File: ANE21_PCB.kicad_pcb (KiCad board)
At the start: 2 copper layers, 128 parts, among them J1 Conn_02x07_Odd_Even, J11 Conn_02x05_Odd_Even, J12 THD-02-R, J13 1-2199119-5, J14 USB_A, J15 USB_OTG, J2 Conn_01x03, J3 Conn_01x03, J4 THD-20-R, J5 690-019-298-412, J8 Molex 470531000, Q1 DMP3013SFV-7, U1 74LVC1G07SE-7, U10 TPD4EUSB30, U11 AP22653W6, U12 SI-51005-F, U13 RT9742SNGV, U2 74LVC1G07SE-7, U4 AP64501SP-13, U5 PCF85063AT/AAZ, U6 EMC2301-1-ACZL-TR, U7 74LVC1G07SE-7, U8 FSUSB42MUX, U9 USB2514B-I/M2, Y1 24MHz, Y2 X32K768S301

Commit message: Added 3d-models, esd protection, cleaned up and made small start with pcb
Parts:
- removed BT1: Battery_Cell, Battery:BatteryHolder_Keystone_3034_1x20mm
- removed C15, C31, C32, C33, C34, C42, C43, C50, C52, C53, C54, C55: 10u, Capacitor_SMD:C_0805_2012Metric
- removed C16, C35, C51: 100uF, Capacitor_Tantalum_SMD:CP_EIA-7343-31_Kemet-D
- removed C17, C18, C19, C20, C22, C23, C27: 10u 35v, Capacitor_SMD:C_0805_2012Metric
- removed C21: 100n 100v, Capacitor_SMD:C_0402_1005Metric
- removed C24, C25, C26, C36, C37, C38, C39, C44, C45, C46, C47, C48, C49: 100n, Capacitor_SMD:C_0402_1005Metric
- removed C28, C30: nf, Capacitor_SMD:C_0402_1005Metric
- removed C29: 1.2nF, Capacitor_SMD:C_0402_1005Metric
- removed C40, C41: 27pF, Capacitor_SMD:C_0402_1005Metric
- removed D2: BAT54C-7-F, Package_TO_SOT_SMD:SOT-23
- removed J11: Conn_02x05_Odd_Even, Connector_PinHeader_2.54mm:PinHeader_2x05_P2.54mm_Vertical
- removed J12: THD-02-R, Connector_PinHeader_2.54mm:PinHeader_2x02_P2.54mm_Vertical
- removed J14: USB_A, Connector_USB:USB_A_Receptacle_XKB_U231-091N-4BLRA00-S
- removed J2: Conn_01x03, Connector_PinHeader_2.54mm:PinHeader_1x03_P2.54mm_Vertical
- removed J8: Molex 470531000, Connector:FanPinHeader_1x04_P2.54mm_Vertical
- removed Module2: ComputeModule4-CM4, ComputeModule4:Raspberry-Pi-4-Compute-Module
- removed Q1: DMP3013SFV-7, Package_SON:Diodes_PowerDI3333-8
- removed R10, R17, R19: 36K 1%, Resistor_SMD:R_0402_1005Metric
- removed R11, R12: 510K 1%, Resistor_SMD:R_0402_1005Metric
- removed R13, R14, R21, R22, R9: 2.2K 1%, Resistor_SMD:R_0402_1005Metric
- removed R18, R8: 12K 1%, Resistor_SMD:R_0402_1005Metric
- removed R20: 15K 1%, Resistor_SMD:R_0402_1005Metric
- removed R7: 20K 1%, Resistor_SMD:R_0402_1005Metric
- removed TP1, TP2, TP3, TP4: TestPoint, TestPoint:TestPoint_Pad_2.0x2.0mm
- removed U5: PCF85063AT/AAZ, Package_SO:SOIC-8_3.9x4.9mm_P1.27mm
- removed U6: EMC2301-1-ACZL-TR, Package_SO:MSOP-8_3x3mm_P0.65mm
- removed U7: 74LVC1G07SE-7, Package_TO_SOT_SMD:SOT-353_SC-70-5
- removed Y1: 24MHz, Crystal:Crystal_SMD_HC49-SD
- removed Y2: X32K768S301, Crystal:Crystal_SMD_3215-2Pin_3.2x1.5mm
- added C59: 100n, Capacitor_SMD:C_0603_1608Metric, F.Cu at (129.6, 72.4)
- added J16: Conn_01x02, Connector_PinHeader_2.54mm:PinHeader_1x02_P2.54mm_Vertical, F.Cu at (150.8, 65.9)
- added J6: SS-52400-004, SS-52400-004 (USB-c connector):STEWART_SS-52400-004 (USB-C), F.Cu at (112.0, 50.3)
- added Module1: ComputeModule4-CM4, ComputeModule4:Raspberry-Pi-4-Compute-Module, F.Cu at (114.4, 126.4)
- added U3: HUSB238_xxxDD, Package_DFN_QFN:WDFN-10-1EP_3x3mm_P0.5mm_EP1.8x2.5mm, F.Cu at (112.5, 59.3)
- C1, C6: value 10u 35v -> 100nF; footprint Capacitor_SMD:C_0805_2012Metric -> Capacitor_SMD:C_0603_1608Metric
- C10: value 1.2nF -> 22uF; footprint Capacitor_SMD:C_0402_1005Metric -> Capacitor_SMD:C_0603_1608Metric
- C11: value nf -> 22uF; footprint Capacitor_SMD:C_0402_1005Metric -> Capacitor_SMD:C_0603_1608Metric
- C12, C13: value 10u -> 22uF; footprint Capacitor_SMD:C_0805_2012Metric -> Capacitor_SMD:C_0603_1608Metric
- C14: value 10u -> 100nF; footprint Capacitor_SMD:C_0805_2012Metric -> Capacitor_SMD:C_0603_1608Metric
- C2: value 10u 35v -> 22µF; footprint Capacitor_SMD:C_0805_2012Metric -> Capacitor_SMD:C_0603_1608Metric
- C3: value 10u 35v -> 1µF; footprint Capacitor_SMD:C_0805_2012Metric -> Capacitor_SMD:C_0603_1608Metric
- C4, C5: value 10u 35v -> 10µF; footprint Capacitor_SMD:C_0805_2012Metric -> Capacitor_SMD:C_0603_1608Metric
- C56, C57: footprint Capacitor_SMD:C_0402_1005Metric -> Capacitor_SMD:C_0603_1608Metric
- C7: value 100n -> 100nF; footprint Capacitor_SMD:C_0402_1005Metric -> Capacitor_SMD:C_0603_1608Metric
- C8: value 100n -> 10pF; footprint Capacitor_SMD:C_0402_1005Metric -> Capacitor_SMD:C_0603_1608Metric
- C9: value nf -> 10pF; footprint Capacitor_SMD:C_0402_1005Metric -> Capacitor_SMD:C_0603_1608Metric
- J1: value Conn_02x07_Odd_Even -> Conn_02x05_Odd_Even
- J3: value Conn_01x03 -> USB-A-S-VT; footprint Connector_PinHeader_2.54mm:PinHeader_1x03_P2.54mm_Vertical -> USB-A-S-VT:CONN_USB-A-S-VT_ADM
- L1, L2: value SRN6045TA-3R3Y -> 3,3uH; footprint Inductor_SMD:L_Bourns_SRN6045TA -> Inductor_SMD:L_0603_1608Metric
- R1, R6: value 10R -> 10K; footprint Resistor_SMD:R_0402_1005Metric -> Resistor_SMD:R_0603_1608Metric
- R15, R16: value 36K 1% -> 330; footprint Resistor_SMD:R_0402_1005Metric -> Resistor_SMD:R_0603_1608Metric
- R2: value 12K 1% -> 22.6K; footprint Resistor_SMD:R_0402_1005Metric -> Resistor_SMD:R_0603_1608Metric
- R23, R26: footprint Resistor_SMD:R_0402_1005Metric -> Resistor_SMD:R_0603_1608Metric
- R3: value 47K 1% -> 31,6K; footprint Resistor_SMD:R_0402_1005Metric -> Resistor_SMD:R_0603_1608Metric
- R4: value 15K 1% -> 10K; footprint Resistor_SMD:R_0402_1005Metric -> Resistor_SMD:R_0603_1608Metric
- R5: value 12K 1% -> 52,3K; footprint Resistor_SMD:R_0402_1005Metric -> Resistor_SMD:R_0603_1608Metric
- U10: value TPD4EUSB30 -> PUSB3FR4; footprint Package_SON:USON-10_2.5x1.0mm_P0.5mm -> lib:SOT1176-1
- U11: value AP22653W6 -> TPD4EUSB30; footprint Package_TO_SOT_SMD:SOT-23-6 -> Package_SON:USON-10_2.5x1.0mm_P0.5mm
- U12: footprint Ethernet_con:TE_RJ45-8L-B -> SI-51005-F:BEL_SI-51005-F
- U4: value AP64501SP-13 -> AP62300WU-7; footprint Package_SO:SOIC-8-1EP_3.9x4.9mm_P1.27mm_EP2.95x4.9mm_Mask2.71x3.4mm_ThermalVias -> AP62300WU-7:SOT95P280X100-6N
- U8: value FSUSB42MUX -> AP62300WU-7; footprint Package_SO:MSOP-10_3x3mm_P0.5mm -> AP62300WU-7:SOT95P280X100-6N
- U9: value USB2514B-I/M2 -> PUSB3FR4; footprint Package_DFN_QFN:QFN-36-1EP_6x6mm_P0.5mm_EP3.7x3.7mm -> lib:SOT1176-1
- moved J4 115.6 mm to (-89.9, 43.4)
- moved J15 111.1 mm to (153.0, 72.5), turned to 90 degrees
- moved J13 102.1 mm to (72.7, 54.3)
- moved U11 92.6 mm to (146.7, 67.8), turned to 180 degrees
- moved U1 85.2 mm to (22.2, 47.4)
- moved U12 84.2 mm to (129.3, 56.0)
- moved U10 79.9 mm to (138.1, 83.0)
- moved J1 79.4 mm to (15.2, 33.9)
- moved U13 74.5 mm to (101.5, 60.9), turned to -90 degrees
- moved R16 73.3 mm to (132.5, 72.0), turned to 90 degrees
- moved C57 70.0 mm to (99.2, 60.9), turned to -90 degrees
- moved U8 67.8 mm to (112.5, 72.9), turned to 180 degrees
- moved C56 67.0 mm to (103.8, 60.9), turned to -90 degrees
- moved H5 66.4 mm to (37.4, 35.0)
- moved H6 66.4 mm to (37.4, 42.0)
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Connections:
- net /GPIO10 renamed /CM4_LowSpeed/GPIO10
- net /GPIO11 renamed /CM4_LowSpeed/GPIO11
- net /GPIO12 renamed /CM4_LowSpeed/GPIO12
- net /GPIO13 renamed /CM4_LowSpeed/GPIO13
- net /GPIO14 renamed /CM4_LowSpeed/GPIO14
- net /GPIO15 renamed /CM4_LowSpeed/GPIO15
- net /GPIO16 renamed /CM4_LowSpeed/GPIO16
- net /GPIO17 renamed /CM4_LowSpeed/GPIO17
- net /GPIO18 renamed /CM4_LowSpeed/GPIO18
- net /GPIO19 renamed /CM4_LowSpeed/GPIO19
- net /GPIO2 renamed /CM4_LowSpeed/GPIO2
- net /GPIO20 renamed /CM4_LowSpeed/GPIO20
- net /GPIO21 renamed /CM4_LowSpeed/GPIO21
- net /GPIO22 renamed /CM4_LowSpeed/GPIO22
- net /GPIO23 renamed /CM4_LowSpeed/GPIO23
- net /GPIO24 renamed /CM4_LowSpeed/GPIO24
- net /GPIO25 renamed /CM4_LowSpeed/GPIO25
- net /GPIO26 renamed /CM4_LowSpeed/GPIO26
- net /GPIO27 renamed /CM4_LowSpeed/GPIO27
- net /GPIO3 renamed /CM4_LowSpeed/GPIO3
- net /GPIO4 renamed /CM4_LowSpeed/GPIO4
- net /GPIO5 renamed /CM4_LowSpeed/GPIO5
- net /GPIO6 renamed /CM4_LowSpeed/GPIO6
- net /GPIO7 renamed /CM4_LowSpeed/GPIO7
- net /GPIO8 renamed /CM4_LowSpeed/GPIO8
- net /GPIO9 renamed /CM4_LowSpeed/GPIO9
- net /ID_SC renamed /CM4_LowSpeed/ID_SC
- net /ID_SD renamed /CM4_LowSpeed/ID_SD
- C1 pad 1: /+12v -> GND
- C1 pad 2: GND -> VIN_U9
- C10 pad 1: Net-(C10-Pad1) -> GND
- C10 pad 2: GND -> +3,3V DC
- C11 pad 1: /PSUs/+3.3v -> GND
- C11 pad 2: Net-(U3-FB) -> +5V DC
- C12 pad 1: /PSUs/+3.3v -> GND
- C12 pad 2: GND -> +3,3V DC
- C13 pad 1: /PSUs/+3.3v -> GND
- C13 pad 2: GND -> +5V DC
- C14 pad 1: /PSUs/+3.3v -> Net-(C14-Pad1)
- C2 pad 1: /+12v -> GND
- C2 pad 2: GND -> VIN_U9
- C3 pad 1: /+12v -> GND
- C3 pad 2: GND -> VIN_U9
- C4 pad 1: /+12v -> VIN_U9
- C5 pad 1: /+12v -> VIN_U9
- C56 pad 1: /+5v -> +5V DC
- C6 pad 1: /+12v -> Net-(U4-BST)
- C6 pad 2: GND -> Net-(U4-SW)
- C7 pad 1: Net-(C7-Pad1) -> Net-(U8-BST)
- C7 pad 2: Net-(U3-BST) -> Net-(U8-SW)
- C8 pad 1: Net-(U3-SS) -> Net-(U4-FB)
- C8 pad 2: GND -> +3,3V DC
- C9 pad 1: Net-(U3-COMP) -> Net-(U8-FB)
- C9 pad 2: GND -> +5V DC
- D3 pad 2: /+3.3v -> +3,3V DC
- D4 pad 2: /+3.3v -> +3,3V DC
- J1 pad 1: GND -> Net-(J1-Pin_1)
- J1 pad 11: /TV_OUT -> (no net)
- J1 pad 12: GND -> (no net)
- J1 pad 13: Net-(J1-Pin_13) -> (no net)
- J1 pad 14: /GLOBAL_EN -> (no net)
- J1 pad 2: /nRPIBOOT -> /GLOBAL_EN
- J1 pad 3: GND -> /WL_nDis
- J1 pad 4: /EEPROM_nWP -> GND
- J1 pad 5: /AIN0 -> /BT_nDis
- J1 pad 6: /AIN1 -> GND
- J1 pad 7: GND -> /nRPIBOOT
- J1 pad 8: /SYNC_IN -> GND
- J1 pad 9: /SYNC_OUT -> /EEPROM_nWP
- J13 pad 12: /CM4_HighSpeed/P7 -> +3,3V DC
- J13 pad 14: /CM4_HighSpeed/P7 -> +3,3V DC
- J13 pad 16: /CM4_HighSpeed/P7 -> +3,3V DC
- J13 pad 18: /CM4_HighSpeed/P7 -> +3,3V DC
- J13 pad 2: /CM4_HighSpeed/P7 -> +3,3V DC
- J13 pad 4: /CM4_HighSpeed/P7 -> +3,3V DC
- J13 pad 50: /CM4_HighSpeed/P7 -> +3,3V DC
- J13 pad 52: /CM4_HighSpeed/P7 -> +3,3V DC
- J13 pad 70: /CM4_HighSpeed/P7 -> +3,3V DC
- J13 pad 72: /CM4_HighSpeed/P7 -> +3,3V DC
- J13 pad 74: /CM4_HighSpeed/P7 -> +3,3V DC
- J15 pad 1: /Ethernet_USB/+5v -> +5V DC
- J15 pad 2: /Ethernet_USB/USB2 -> pUSBD-
- J15 pad 3: /Ethernet_USB/USB3 -> pUSBD+
- J15 pad 4: /Ethernet_USB/USB1 -> USB_OTG
- J3 pad 1: /GLOBAL_EN -> +5V DC
- J3 pad 2: GND -> pUSBD-
- J3 pad 3: /RUN_PG -> pUSBD+
- J4 pad 1: /+3.3v -> +3,3V DC
- J4 pad 17: /+3.3v -> +3,3V DC
- J4 pad 2: /+5v -> /CM4_LowSpeed/+5v
- J4 pad 4: /+5v -> /CM4_LowSpeed/+5v
- L1 pad 2: /+5v -> +3,3V DC
- L2 pad 1: Net-(U3-SW) -> Net-(U8-SW)
- L2 pad 2: /PSUs/+3.3v -> +5V DC
- R1 pad 1: Net-(U3-SW) -> Net-(U3-VSET)
- R1 pad 2: Net-(C7-Pad1) -> GND
- R15 pad 1: Net-(U9-SCL/SMBCLK/CFG_SEL0) -> /CM4_LowSpeed/E9
- R15 pad 2: GND -> Net-(U12-LEDR_K)
- R16 pad 1: Net-(U9-SDA/SMBDATA/NON_REM1) -> Net-(U12-LEDL_K)
- R16 pad 2: GND -> /CM4_LowSpeed/E10
- R2 pad 1: Net-(U3-COMP) -> Net-(U3-ISET)
- R2 pad 2: Net-(C10-Pad1) -> GND
- R23 pad 1: Net-(D3-K) -> Net-(Module1A-PI_nLED_Activity)
- R23 pad 2: Net-(Module3A-PI_nLED_Activity) -> Net-(D3-K)
- R3 pad 1: /PSUs/+3.3v -> +3,3V DC
- R3 pad 2: Net-(U3-FB) -> Net-(U4-FB)
- R4 pad 1: Net-(U3-FB) -> Net-(U4-FB)
- R5 pad 1: Net-(D1-A) -> +5V DC
- R5 pad 2: GND -> Net-(U8-FB)
- R6 pad 1: Net-(U4-SW) -> Net-(U8-FB)
- R6 pad 2: Net-(C24-Pad1) -> GND
- U1 pad 4: Net-(J1-Pin_13) -> Net-(J1-Pin_1)
- U10 pad 1: Net-(U10-D1+) -> unconnected-(U10-In_1+-Pad1)
- U10 pad 10: Net-(U10-D1+) -> unconnected-(U10-Out_1+-Pad10)
- U10 pad 2: Net-(U10-D1-) -> unconnected-(U10-In_1--Pad2)
- U10 pad 3: GND -> unconnected-(U10-GND-Pad3)
- U10 pad 4: /USB2-HUB/USBD_N -> unconnected-(U10-In_1+-Pad4)
- U10 pad 5: /USB2-HUB/USBD_P -> unconnected-(U10-In_1--Pad5)
- U10 pad 6: /USB2-HUB/USBD_P -> unconnected-(U10-Out_1+-Pad6)
- U10 pad 7: /USB2-HUB/USBD_N -> unconnected-(U10-Out_1+-Pad7)
- U10 pad 8: GND -> unconnected-(U10-GND-Pad8)
- U10 pad 9: Net-(U10-D1-) -> unconnected-(U10-Out_1+-Pad9)
- U11 pad 1: /+5v -> USBD+
- U11 pad 2: GND -> USBD-
- U11 pad 3: /USB2-HUB/PWR1 -> GND
- U11 pad 4: /USB2-HUB/nOCS1 -> pUSBD+
- U11 pad 5: Net-(U11-ILIM) -> pUSBD-
- U11 pad 6: /USB2-HUB/VBUS -> pUSBD-
- U12 pad 2: /Ethernet_USB/E1 -> /CM4_LowSpeed/E1
- U12 pad 3: /Ethernet_USB/E2 -> /CM4_LowSpeed/E2
- U12 pad 4: /Ethernet_USB/E3 -> /CM4_LowSpeed/E3
- U12 pad 5: /Ethernet_USB/E4 -> /CM4_LowSpeed/E4
- U12 pad 7: /Ethernet_USB/E5 -> /CM4_LowSpeed/E5
- U12 pad 8: /Ethernet_USB/E6 -> /CM4_LowSpeed/E6
- U13 pad 1: /+5v -> +5V DC
- U2 pad 2: /nPWR_LED -> /CM4_LowSpeed/nPWR_LED
- U2 pad 5: /+3.3v -> +3,3V DC
- U4 pad 1: Net-(U4-BST) -> GND
- U4 pad 2: /+12v -> Net-(U4-SW)
- U4 pad 3: /+12v -> VIN_U9
- U4 pad 4: Net-(U4-SS) -> Net-(U4-FB)
- U4 pad 5: Net-(U4-FB) -> unconnected-(U4-EN-Pad5)
- U4 pad 6: Net-(U4-COMP) -> Net-(U4-BST)
- U8 pad 1: /+3.3v -> GND
- U8 pad 2: /USB2-HUB/USBOTG -> Net-(U8-SW)
- U8 pad 3: /USB2-HUB/USB2_P -> VIN_U9
- U8 pad 4: /USB2-HUB/USB2_N -> Net-(U8-FB)
- U8 pad 5: GND -> unconnected-(U8-EN-Pad5)
- U8 pad 6: /USB2-HUB/USBH_N -> Net-(U8-BST)
- U9 pad 1: /USB2-HUB/HD1_N -> unconnected-(U9-In_1+-Pad1)
- U9 pad 10: /+3.3v -> unconnected-(U9-Out_1+-Pad10)
- U9 pad 2: /USB2-HUB/HD1_P -> unconnected-(U9-In_1--Pad2)
- U9 pad 3: /USB2-HUB/HD2_N -> unconnected-(U9-GND-Pad3)
- U9 pad 4: /USB2-HUB/HD2_P -> unconnected-(U9-In_1+-Pad4)
- U9 pad 5: /+3.3v -> unconnected-(U9-In_1--Pad5)
- U9 pad 6: /USB2-HUB/HD3_N -> unconnected-(U9-Out_1+-Pad6)
- U9 pad 7: /USB2-HUB/HD3_P -> unconnected-(U9-Out_1+-Pad7)
- U9 pad 8: /USB2-HUB/HD4_N -> unconnected-(U9-GND-Pad8)
- U9 pad 9: /USB2-HUB/HD4_P -> unconnected-(U9-Out_1+-Pad9)
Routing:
- net Net-(U4-SW): track 0.00 -> 5.60 mm
- net Net-(U4-FB): track 0.00 -> 4.66 mm
- net Net-(U8-FB): track 0.00 -> 4.07 mm
- net Net-(U8-SW): track 0.00 -> 3.80 mm
- net +3,3V DC: track 0.00 -> 3.32 mm
- net Net-(U4-BST): track 0.00 -> 2.32 mm
- net Net-(U8-BST): track 0.00 -> 2.09 mm
- added copper zone on B.Cu, net GND
- added copper zone on F.Cu, net GND
- removed copper zone on B.Cu, net (none)
- removed copper zone on F.Cu, net (none)
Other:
- board outline added: 95.2 x 95.2 mm

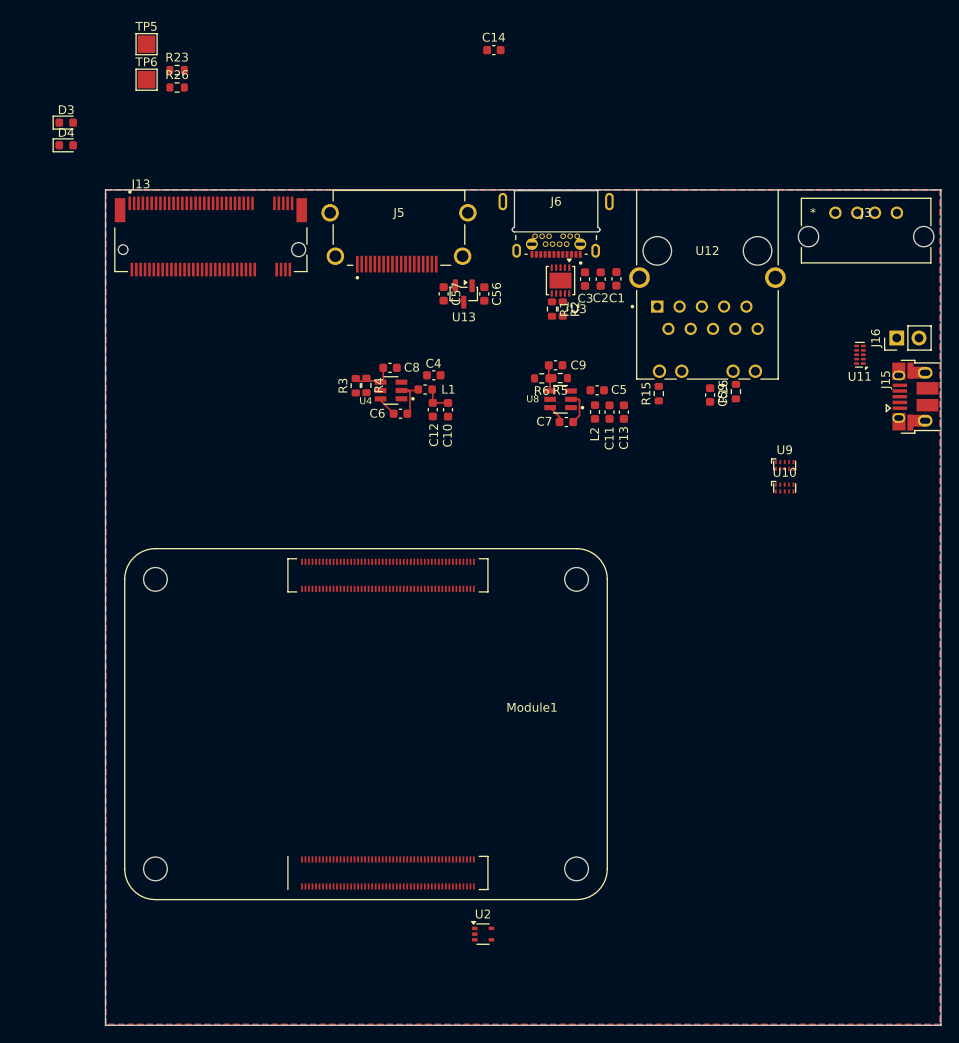
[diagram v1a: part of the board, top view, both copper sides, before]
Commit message: Adjusted the PCB design, changed footprints to 0402 (temp)
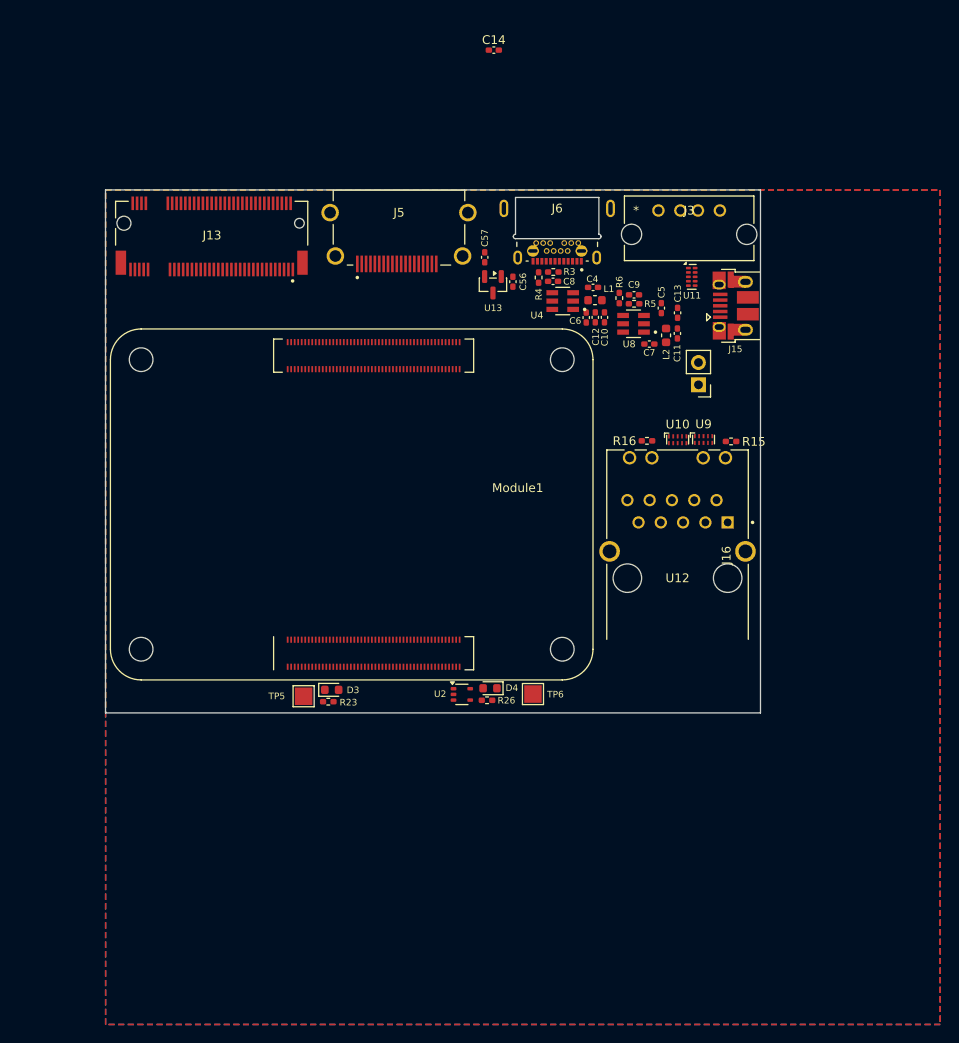
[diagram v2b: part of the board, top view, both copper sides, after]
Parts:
- removed C1: 100nF, Capacitor_SMD:C_0603_1608Metric
- removed C2: 22µF, Capacitor_SMD:C_0603_1608Metric
- removed C3: 1µF, Capacitor_SMD:C_0603_1608Metric
- removed C59: 100n, Capacitor_SMD:C_0603_1608Metric
- removed R1: 10K, Resistor_SMD:R_0603_1608Metric
- removed R2: 22.6K, Resistor_SMD:R_0603_1608Metric
- removed U3: HUSB238_xxxDD, Package_DFN_QFN:WDFN-10-1EP_3x3mm_P0.5mm_EP1.8x2.5mm
- C10, C11, C12, C13, C14, C4, C5, C56, C57, C6, C7, C8, C9: footprint Capacitor_SMD:C_0603_1608Metric -> Capacitor_SMD:C_0402_1005Metric_Pad0.74x0.62mm_HandSolder
- R15, R16, R23, R26, R3, R4, R5, R6: footprint Resistor_SMD:R_0603_1608Metric -> Resistor_SMD:R_0402_1005Metric_Pad0.72x0.64mm_HandSolder
- moved TP6 82.7 mm to (109.4, 106.5)
- moved D4 78.5 mm to (104.5, 105.8), turned to 180 degrees
- moved R26 78.3 mm to (104.2, 107.2), turned to 180 degrees
- moved TP5 76.4 mm to (83.2, 106.7)
- moved R23 74.0 mm to (86.1, 107.3), turned to 180 degrees
- moved D3 71.4 mm to (86.5, 106.0)
- moved U12 37.5 mm to (125.9, 93.2), turned to 0 degrees
- moved U2 27.4 mm to (101.3, 106.5)
- moved R3 26.0 mm to (111.7, 58.4), turned to 180 degrees
- moved Module1 25.1 mm to (112.7, 101.3)
- moved C6 23.8 mm to (115.5, 63.5), turned to 90 degrees
- moved J16 23.2 mm to (128.2, 71.2), turned to 180 degrees
- moved R4 23.2 mm to (110.0, 59.0)
- moved J15 22.9 mm to (132.5, 62.2)
- moved U4 22.1 mm to (112.8, 61.7)
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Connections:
- U10 pad 1: unconnected-(U10-In_1+-Pad1) -> /CM4_LowSpeed/E8
- U10 pad 10: unconnected-(U10-Out_1+-Pad10) -> /CM4_LowSpeed/E8
- U10 pad 2: unconnected-(U10-In_1--Pad2) -> /CM4_LowSpeed/E7
- U10 pad 3: unconnected-(U10-GND-Pad3) -> GND
- U10 pad 4: unconnected-(U10-In_1+-Pad4) -> /CM4_LowSpeed/E6
- U10 pad 5: unconnected-(U10-In_1--Pad5) -> /CM4_LowSpeed/E5
- U10 pad 6: unconnected-(U10-Out_1+-Pad6) -> /CM4_LowSpeed/E5
- U10 pad 7: unconnected-(U10-Out_1+-Pad7) -> /CM4_LowSpeed/E6
- U10 pad 8: unconnected-(U10-GND-Pad8) -> GND
- U10 pad 9: unconnected-(U10-Out_1+-Pad9) -> /CM4_LowSpeed/E7
- U12 pad 6: Net-(U12-CT) -> unconnected-(U12-CT-Pad6)
- U9 pad 1: unconnected-(U9-In_1+-Pad1) -> /CM4_LowSpeed/E4
- U9 pad 10: unconnected-(U9-Out_1+-Pad10) -> /CM4_LowSpeed/E4
- U9 pad 2: unconnected-(U9-In_1--Pad2) -> /CM4_LowSpeed/E3
- U9 pad 3: unconnected-(U9-GND-Pad3) -> GND
- U9 pad 4: unconnected-(U9-In_1+-Pad4) -> /CM4_LowSpeed/E2
- U9 pad 5: unconnected-(U9-In_1--Pad5) -> /CM4_LowSpeed/E1
- U9 pad 6: unconnected-(U9-Out_1+-Pad6) -> /CM4_LowSpeed/E1
- U9 pad 7: unconnected-(U9-Out_1+-Pad7) -> /CM4_LowSpeed/E2
- U9 pad 8: unconnected-(U9-GND-Pad8) -> GND
- U9 pad 9: unconnected-(U9-Out_1+-Pad9) -> /CM4_LowSpeed/E3
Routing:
- net Net-(U4-SW): track 5.60 -> 0.00 mm
- net Net-(U4-FB): track 4.66 -> 0.00 mm
- net Net-(U8-FB): track 4.07 -> 0.00 mm
- net Net-(U8-SW): track 3.80 -> 0.00 mm
- net +3,3V DC: track 3.32 -> 0.00 mm
- net Net-(U4-BST): track 2.32 -> 0.00 mm
- net Net-(U8-BST): track 2.09 -> 0.00 mm
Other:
- board size 95.2 x 95.2 mm -> 74.6 x 59.6 mm

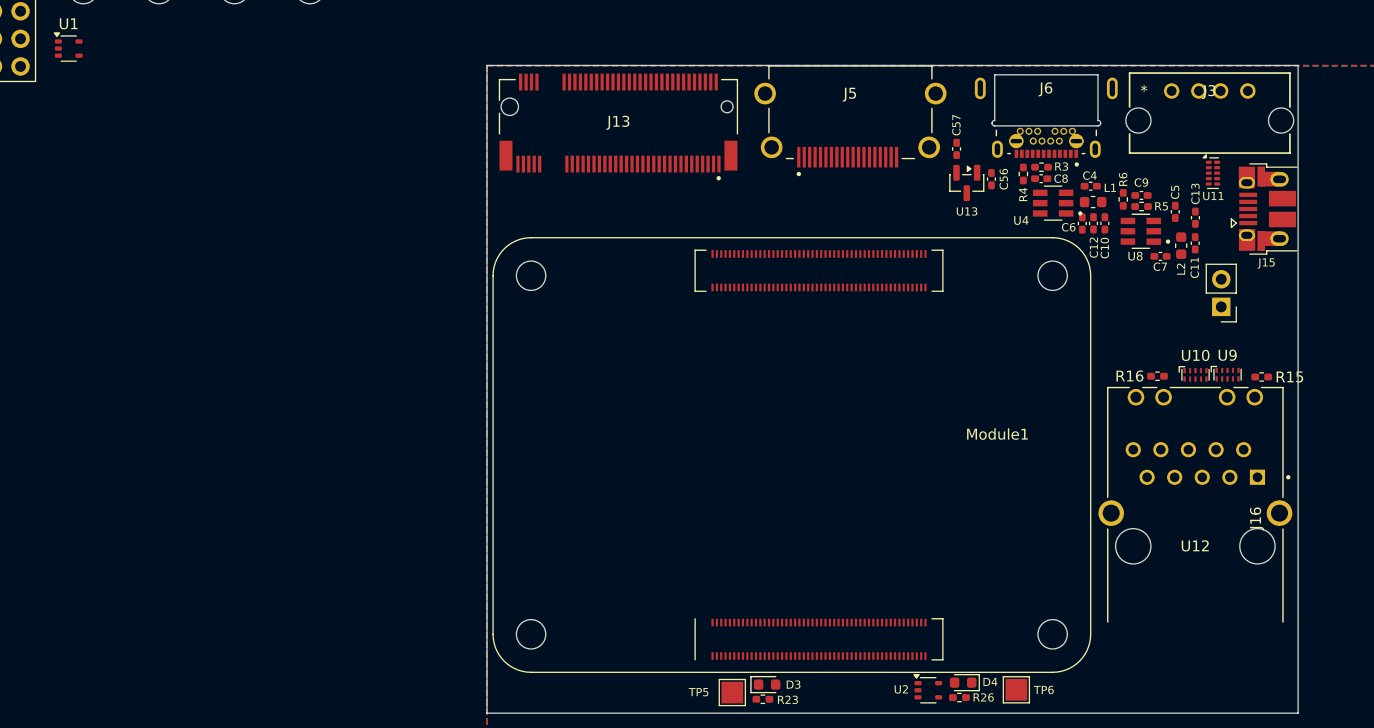
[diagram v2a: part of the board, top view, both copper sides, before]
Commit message: Adjusted netclasses to route differential pairs for PCIe and HDMI. And used JLCPCB to adjust trace width for those
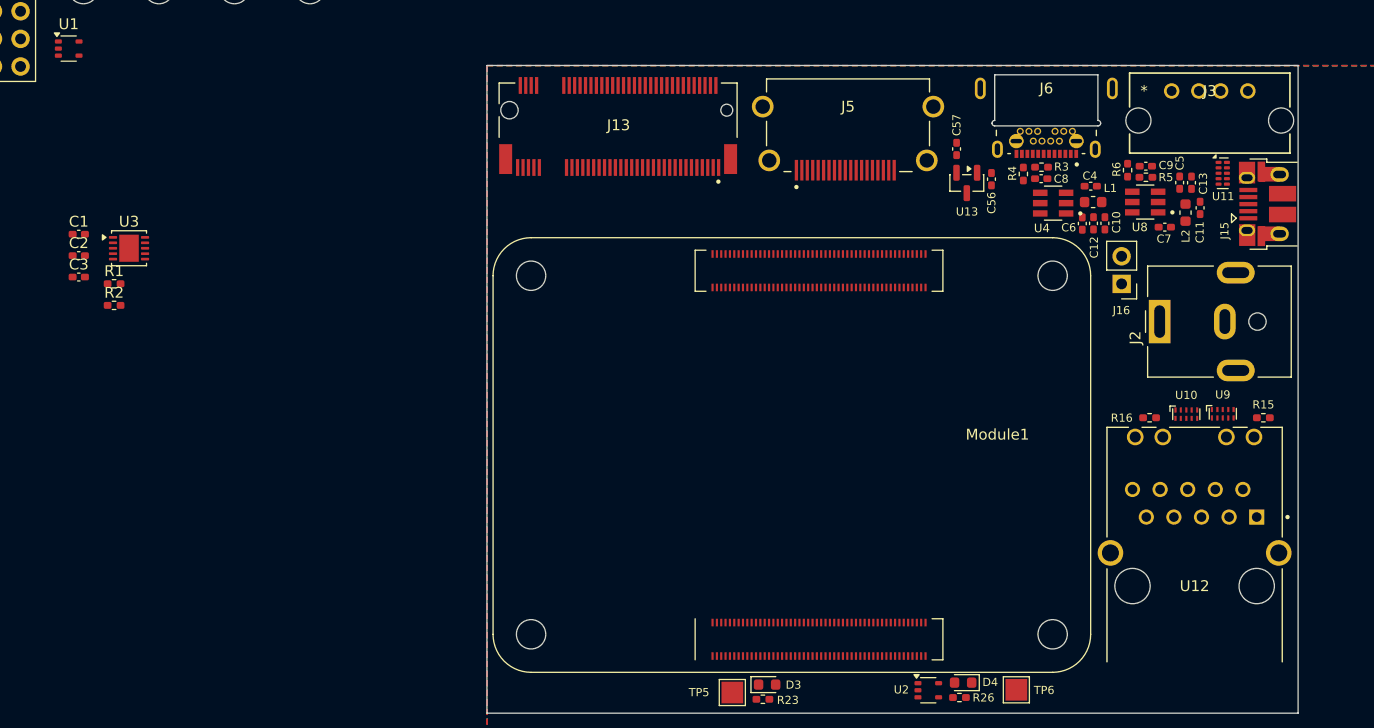
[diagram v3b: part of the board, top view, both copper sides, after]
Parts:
- added C1: 100nF, Capacitor_SMD:C_0402_1005Metric_Pad0.74x0.62mm_HandSolder, F.Cu at (23.1, 64.5)
- added C2: 22µF, Capacitor_SMD:C_0402_1005Metric_Pad0.74x0.62mm_HandSolder, F.Cu at (23.1, 66.5)
- added C3: 1µF, Capacitor_SMD:C_0402_1005Metric_Pad0.74x0.62mm_HandSolder, F.Cu at (23.1, 68.5)
- added J2: Barrel_Jack, Connector_BarrelJack:BarrelJack_CUI_PJ-063AH_Horizontal, F.Cu at (122.6, 72.6)
- added R1: 10K, Resistor_SMD:R_0402_1005Metric_Pad0.72x0.64mm_HandSolder, F.Cu at (26.4, 69.1)
- added R2: 22.6K, Resistor_SMD:R_0402_1005Metric_Pad0.72x0.64mm_HandSolder, F.Cu at (26.4, 71.1)
- added U3: HUSB238_xxxDD, Package_DFN_QFN:WDFN-10-1EP_3x3mm_P0.5mm_EP1.8x2.5mm, F.Cu at (27.7, 65.8)
- moved J16 9.41 mm to (119.1, 69.1)
- moved R16 3.89 mm to (121.7, 81.4)
- moved R15 3.75 mm to (132.1, 81.4)
- moved U10 3.72 mm to (125.0, 81.1)
- moved U12 3.66 mm to (125.8, 96.9)
- moved U9 3.63 mm to (128.4, 81.1)
- moved C11 3.29 mm to (126.3, 62.1)
- moved C13 3.24 mm to (125.5, 59.8)
- moved L2 3.07 mm to (125.0, 62.5)
- moved U8 2.72 mm to (121.2, 61.6)
- moved C5 2.72 mm to (124.4, 59.8)
- moved C9 2.72 mm to (121.3, 58.3)
- moved R5 2.72 mm to (121.3, 59.3)
- moved R6 2.72 mm to (119.6, 58.6)
- moved C7 2.72 mm to (123.1, 63.9)
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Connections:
- net /CM4_HighSpeed/H1 renamed /CM4_HighSpeed/HDMI0_D2_P
- net /CM4_HighSpeed/H10 renamed /CM4_HighSpeed/HDMI0_SCL
- net /CM4_HighSpeed/H11 renamed /CM4_HighSpeed/HDMI0_SDA
- net /CM4_HighSpeed/H12 renamed /CM4_HighSpeed/HDMI0_HOT
- net /CM4_HighSpeed/H2 renamed /CM4_HighSpeed/HDMI0_D2_N
- net /CM4_HighSpeed/H3 renamed /CM4_HighSpeed/HDMI0_D1_P
- net /CM4_HighSpeed/H4 renamed /CM4_HighSpeed/HDMI0_D1_N
- net /CM4_HighSpeed/H5 renamed /CM4_HighSpeed/HDMI0_D0_P
- net /CM4_HighSpeed/H6 renamed /CM4_HighSpeed/HDMI0_D0_N
- net /CM4_HighSpeed/H7 renamed /CM4_HighSpeed/HDMI0_CK_P
- net /CM4_HighSpeed/H8 renamed /CM4_HighSpeed/HDMI0_CK_N
- net /CM4_HighSpeed/H9 renamed /CM4_HighSpeed/HDMI0_CEC
- net /CM4_HighSpeed/P1 renamed /CM4_HighSpeed/P_RX0_N
- net /CM4_HighSpeed/P2 renamed /CM4_HighSpeed/P_RX0_P
- net /CM4_HighSpeed/P3 renamed /CM4_HighSpeed/P_TX0_N
- net /CM4_HighSpeed/P4 renamed /CM4_HighSpeed/P_TX0_P
- net /CM4_HighSpeed/P5 renamed /CM4_HighSpeed/P_CLK_N
- net /CM4_HighSpeed/P6 renamed /CM4_HighSpeed/P_CLK_P
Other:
- copper layers 2 -> 4
